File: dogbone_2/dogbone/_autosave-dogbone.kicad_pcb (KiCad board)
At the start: 2 copper layers, 23 x 27.4 mm, 11 parts, among them J1 jstsh5x1, U1 TLV2771CDBVT

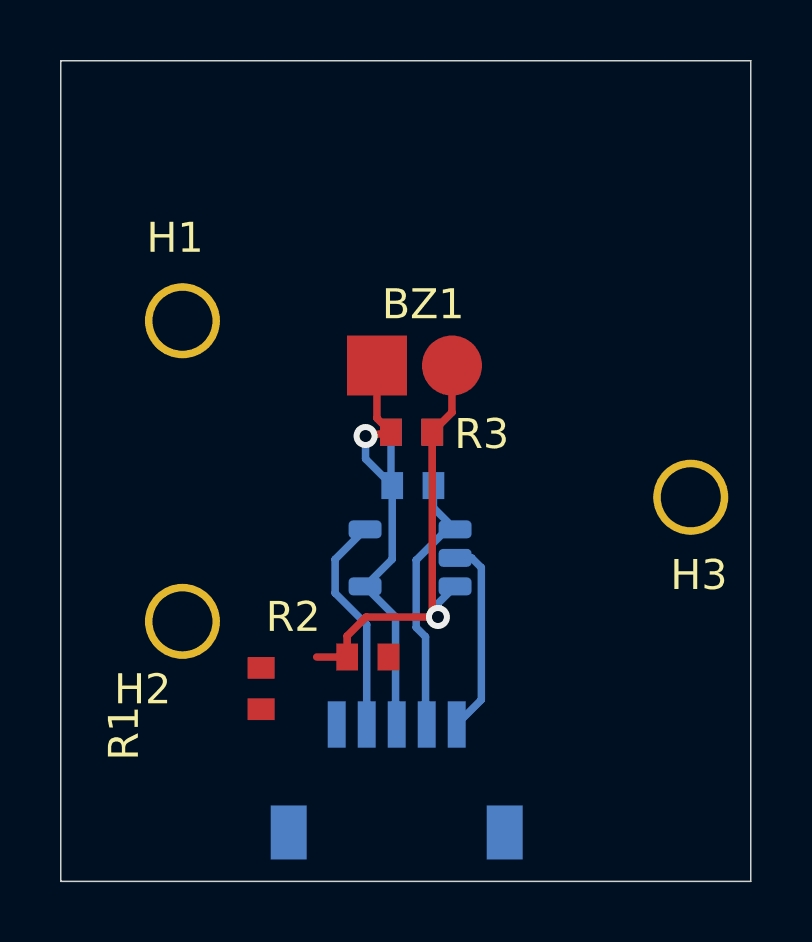
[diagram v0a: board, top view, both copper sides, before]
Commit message: updated dog bone schematic
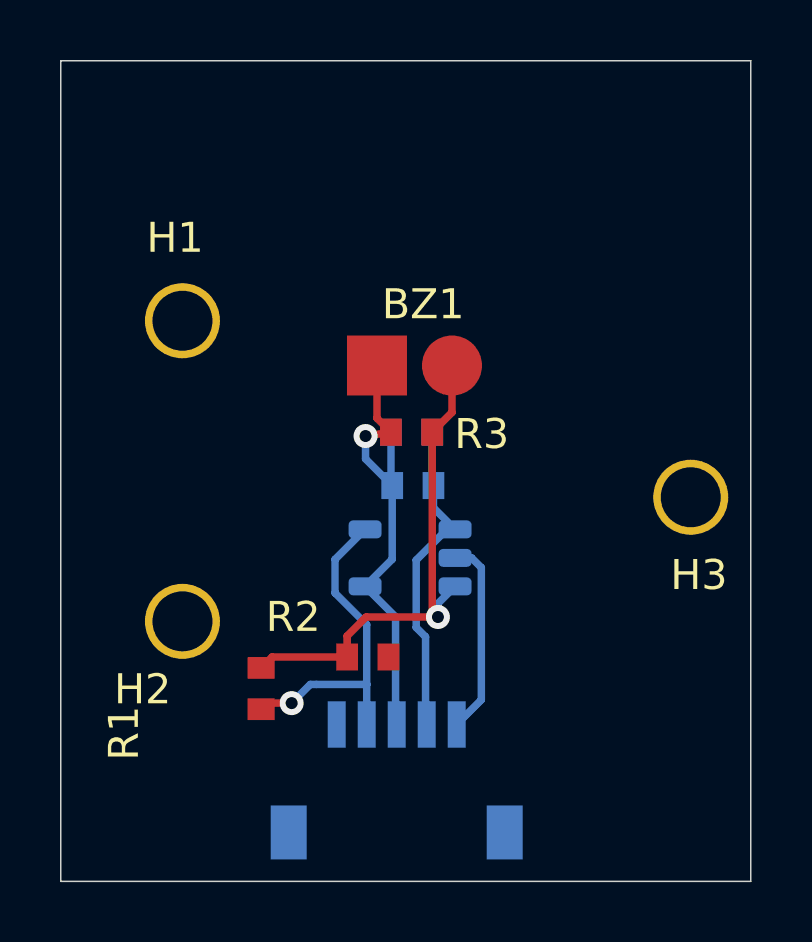
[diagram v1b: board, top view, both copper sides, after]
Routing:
- net +3V3: track 7.35 -> 11.2 mm, vias 0 -> 1
- net VGND: track 15.0 -> 17.0 mm
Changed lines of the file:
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@@
     (thickness 1.6)
     (drawings 4)
-    (tracks 44)
+    (tracks 53)
     (zones 0)
     (modules 11)
@@
       (outputformat 1)
       (mirror false)
-      (drillshape 1)
+      (drillshape 0)
       (scaleselection 1)
-      (outputdirectory ""))
+      (outputdirectory "grbl_output/"))
   )
   (net 0 "")
@@
   (gr_line (start 44.577 76.073) (end 67.577 76.073) (layer Edge.Cuts) (width 0.05))
   (gr_line (start 44.577 76.073) (end 44.577 103.427) (layer Edge.Cuts) (width 0.05))
-  (segment (start 54.124 95.9485) (end 53.108 95.9485) (width 0.25) (layer F.Cu) (net 1))
   (segment (start 54.124 95.2485) (end 54.7575 94.615) (width 0.25) (layer F.Cu) (net 1))
   (segment (start 54.124 95.9485) (end 54.124 95.2485) (width 0.25) (layer F.Cu) (net 1))
@@
   (segment (start 56.9595 94.4245) (end 57.15 94.615) (width 0.25) (layer F.Cu) (net 1))
   (segment (start 56.9595 88.4555) (end 56.9595 94.4245) (width 0.25) (layer F.Cu) (net 1))
+  (segment (start 51.6221 95.9485) (end 51.2572 96.3134) (width 0.25) (layer F.Cu) (net 1))
+  (segment (start 54.124 95.9485) (end 51.6221 95.9485) (width 0.25) (layer F.Cu) (net 1))
   (segment (start 55.5845 90.192) (end 55.626 90.2335) (width 0.25) (layer B.Cu) (net 2))
   (segment (start 55.5845 88.4555) (end 55.5845 90.192) (width 0.25) (layer B.Cu) (net 2))
@@
   (segment (start 53.721 93.815268) (end 53.721 92.6945) (width 0.25) (layer B.Cu) (net 5))
   (segment (start 54.7756 94.869868) (end 53.721 93.815268) (width 0.25) (layer B.Cu) (net 5))
-  (segment (start 54.7756 98.1964) (end 54.7756 94.869868) (width 0.25) (layer B.Cu) (net 5))
+  (segment (start 54.7756 96.8624) (end 53.0992 96.8624) (width 0.25) (layer B.Cu) (net 5))
+  (segment (start 54.7756 98.1964) (end 54.7756 96.8624) (width 0.25) (layer B.Cu) (net 5))
+  (segment (start 54.7756 96.8624) (end 54.7756 94.869868) (width 0.25) (layer B.Cu) (net 5))
+  (segment (start 53.0992 96.8624) (end 52.896 96.8624) (width 0.25) (layer B.Cu) (net 5))
+  (segment (start 52.896 96.8624) (end 52.2732 97.4852) (width 0.25) (layer B.Cu) (net 5))
+  (segment (start 52.2732 97.4852) (end 52.2732 97.4852) (width 0.25) (layer B.Cu) (net 5))
+  (via (at 52.2732 97.4852) (size 0.8) (drill 0.4) (layers F.Cu B.Cu) (net 5))
+  (segment (start 51.4604 97.4852) (end 51.2572 97.6884) (width 0.25) (layer F.Cu) (net 5))
+  (segment (start 52.2732 97.4852) (end 51.4604 97.4852) (width 0.25) (layer F.Cu) (net 5))
   (segment (start 58.2715 92.644) (end 57.7215 92.644) (width 0.25) (layer B.Cu) (net 6))
   (segment (start 58.59651 92.96901) (end 58.2715 92.644) (width 0.25) (layer B.Cu) (net 6))
